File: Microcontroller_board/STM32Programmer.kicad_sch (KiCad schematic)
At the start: 0 parts

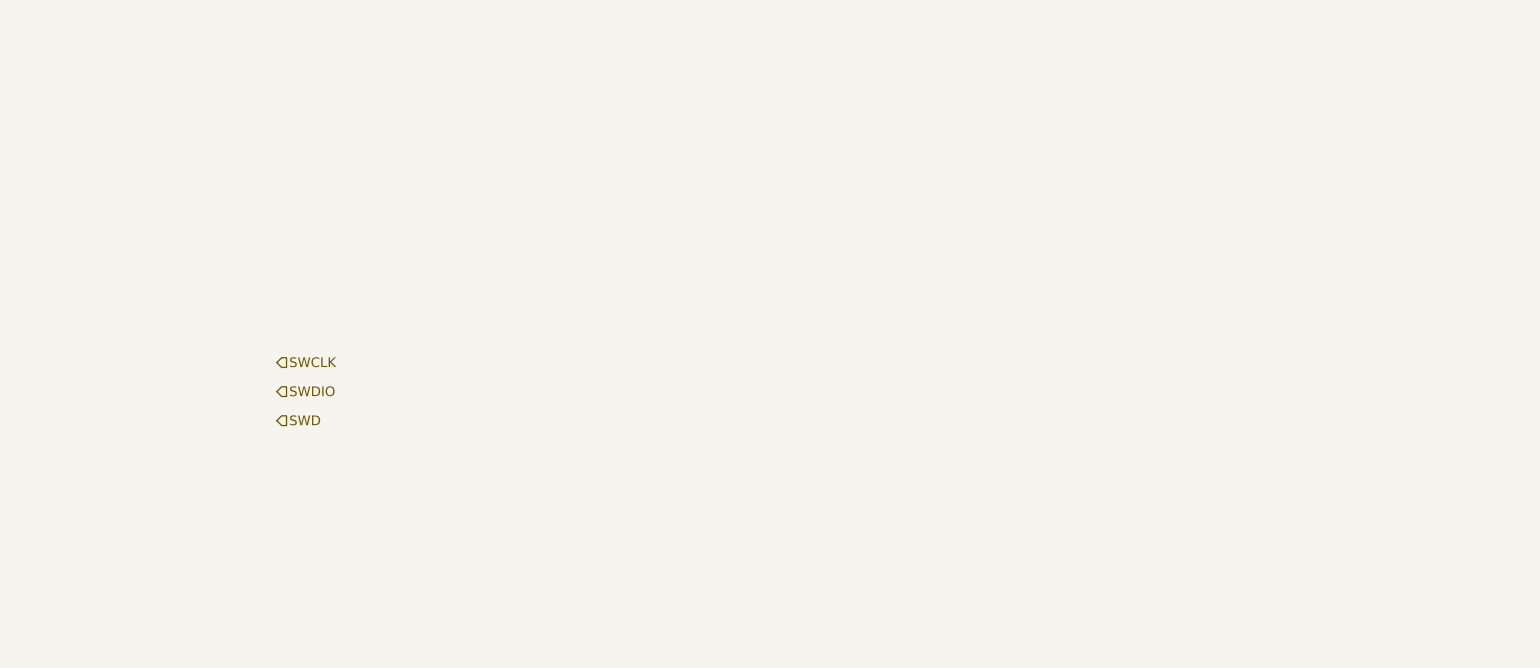
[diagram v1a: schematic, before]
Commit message: Added connector for st link programmer
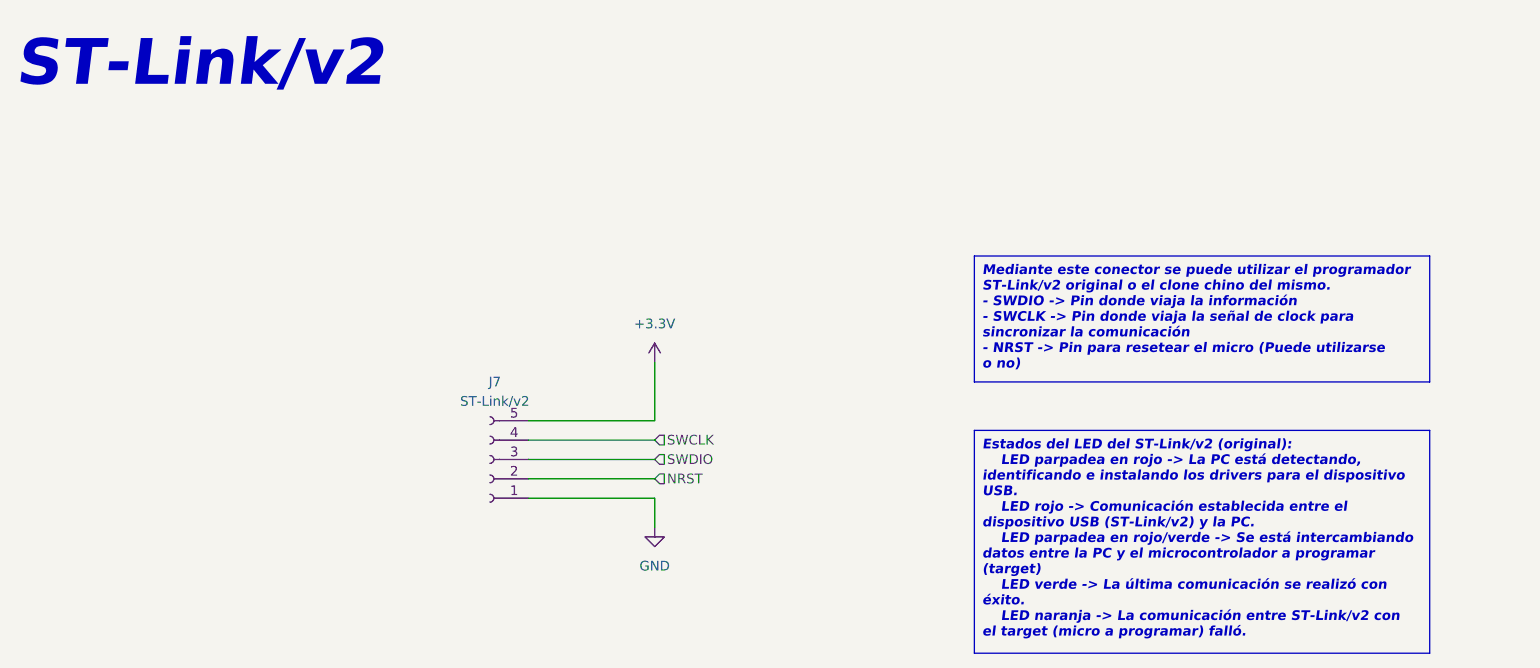
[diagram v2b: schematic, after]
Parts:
- added J7: ST-Link/v2, symbol Connector:Conn_01x05_Socket
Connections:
- net SWCLK: now also J7.4 (Pin_4)
- net SWDIO: now also J7.3 (Pin_3)
- new net +3.3V: J7.5 (Pin_5)
- new net GND: J7.1 (Pin_1)
- new net NRST: J7.2 (Pin_2)
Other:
- note added: "ST-Link/v2"
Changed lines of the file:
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@@
 (kicad_sch (version 20230121) (generator eeschema)
   (paper "A4")
-  (hierarchical_label "SWD" (shape input) (at 60.96 76.2 0) (fields_autoplaced)
+  (wire (pts (xy 110.49 76.2) (xy 110.49 68.58))
+    (stroke (width 0) (type default))
+  )
+  (wire (pts (xy 93.98 78.74) (xy 110.49 78.74))
+    (stroke (width 0) (type default))
+  )
+  (wire (pts (xy 93.98 76.2) (xy 110.49 76.2))
+    (stroke (width 0) (type default))
+  )
+  (wire (pts (xy 93.98 83.82) (xy 110.49 83.82))
+    (stroke (width 0) (type default))
+  )
+  (wire (pts (xy 93.98 81.28) (xy 110.49 81.28))
+    (stroke (width 0) (type default))
+  )
+  (wire (pts (xy 110.49 86.36) (xy 110.49 90.17))
+    (stroke (width 0) (type default))
+  )
+  (wire (pts (xy 93.98 86.36) (xy 110.49 86.36))
+    (stroke (width 0) (type default))
+  )
+  (text_box "Mediante este conector se puede utilizar el programador ST-Link/v2 original o el clone chino del mismo.\n- SWDIO -> Pin donde viaja la información\n- SWCLK -> Pin donde viaja la señal de clock para sincronizar la comunicación\n- NRST -> Pin para resetear el micro (Puede utilizarse o no)"
+    (at 152.4 54.61 0) (size 59.69 16.51)
+    (stroke (width 0) (type default))
+    (fill (type color) (color 255 227 142 1))
+    (effects (font (size 1.27 1.27) bold italic) (justify left top))
+  )
+  (text_box "Estados del LED del ST-Link/v2 (original):\n	LED parpadea en rojo -> La PC está detectando, identificando e instalando los drivers para el dispositivo USB.\n	LED rojo -> Comunicación establecida entre el dispositivo USB (ST-Link/v2) y la PC.\n	LED parpadea en rojo/verde -> Se está intercambiando datos entre la PC y el microcontrolador a programar (target)\n	LED verde -> La última comunicación se realizó con éxito.\n	LED naranja -> La comunicación entre ST-Link/v2 con el target (micro a programar) falló."
+    (at 152.4 77.47 0) (size 59.69 29.21)
+    (stroke (width 0) (type default))
+    (fill (type color) (color 255 227 142 1))
+    (effects (font (size 1.27 1.27) bold italic) (justify left top))
+  )
+  (text "ST-Link/v2" (at 26.67 33.02 0)
+    (effects (font (size 6 6) (thickness 1.2) bold italic) (justify left bottom))
+  )
+  (hierarchical_label "SWCLK" (shape input) (at 110.49 78.74 0) (fields_autoplaced)
     (effects (font (size 1.27 1.27)) (justify left))
   )
-  (hierarchical_label "SWCLK" (shape input) (at 60.96 68.58 0) (fields_autoplaced)
+  (hierarchical_label "SWDIO" (shape input) (at 110.49 81.28 0) (fields_autoplaced)
     (effects (font (size 1.27 1.27)) (justify left))
   )
-  (hierarchical_label "SWDIO" (shape input) (at 60.96 72.39 0) (fields_autoplaced)
+  (hierarchical_label "NRST" (shape input) (at 110.49 83.82 0) (fields_autoplaced)
     (effects (font (size 1.27 1.27)) (justify left))
   )
+  (symbol (lib_id "Connector:Conn_01x05_Socket") (at 88.9 81.28 180) (unit 1)
+    (in_bom yes) (on_board yes) (dnp no) (fields_autoplaced)
+    (property "Reference" "J7" (at 89.535 71.12 0)
+      (effects (font (size 1.27 1.27)))
+    )
+    (property "Value" "ST-Link/v2" (at 89.535 73.66 0)
+      (effects (font (size 1.27 1.27)))
+    )
+    (property "Footprint" "" (at 88.9 81.28 0)
+      (effects (font (size 1.27 1.27)) hide)
+    )
+    (property "Datasheet" "~" (at 88.9 81.28 0)
+      (effects (font (size 1.27 1.27)) hide)
+    )
+    (pin "1")
+    (pin "2")
+    (pin "3")
+    (pin "4")
+    (pin "5")
+    (instances
+      (project "Microcontroller_board"
+        (path "/8159cf7c-7477-4d57-9227-35cab5afcf8d/74c828e6-688c-4762-a2dc-1edaf686966d"
+          (reference "J7") (unit 1)
+        )
+      )
+    )
+  )
+  (symbol (lib_id "power:GND") (at 110.49 90.17 0) (unit 1)
+    (in_bom yes) (on_board yes) (dnp no) (fields_autoplaced)
+    (property "Reference" "#PWR048" (at 110.49 96.52 0)
+      (effects (font (size 1.27 1.27)) hide)
+    )
+    (property "Value" "GND" (at 110.49 95.25 0)
+      (effects (font (size 1.27 1.27)))
+    )
+    (property "Footprint" "" (at 110.49 90.17 0)
+      (effects (font (size 1.27 1.27)) hide)
+    )
+    (property "Datasheet" "" (at 110.49 90.17 0)
+      (effects (font (size 1.27 1.27)) hide)
+    )
+    (pin "1")
+    (instances
+      (project "Microcontroller_board"
+        (path "/8159cf7c-7477-4d57-9227-35cab5afcf8d/74c828e6-688c-4762-a2dc-1edaf686966d"
+          (reference "#PWR048") (unit 1)
+        )
+      )
+    )
+  )
+  (symbol (lib_id "power:+3.3V") (at 110.49 68.58 0) (unit 1)
+    (in_bom yes) (on_board yes) (dnp no) (fields_autoplaced)
+    (property "Reference" "#PWR047" (at 110.49 72.39 0)
+      (effects (font (size 1.27 1.27)) hide)
+    )
+    (property "Value" "+3.3V" (at 110.49 63.5 0)
+      (effects (font (size 1.27 1.27)))
+    )
+    (property "Footprint" "" (at 110.49 68.58 0)
+      (effects (font (size 1.27 1.27)) hide)
+    )
+    (property "Datasheet" "" (at 110.49 68.58 0)
+      (effects (font (size 1.27 1.27)) hide)
+    )
+    (pin "1")
+    (instances
+      (project "Microcontroller_board"
+        (path "/8159cf7c-7477-4d57-9227-35cab5afcf8d/74c828e6-688c-4762-a2dc-1edaf686966d"
+          (reference "#PWR047") (unit 1)
+        )
+      )
+    )
+  )
 )
